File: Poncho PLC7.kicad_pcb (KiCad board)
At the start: 4 copper layers, 135.6 x 54.6 mm, 88 parts, among them J1 TB_1X2, J10 Conn_02x12_Odd_Even, J11 TB_1X2, J12 TB_1X3-PonchoPLC-rescue, J13 Conn_02x05_Odd_Even, J18 Conn_02x05_Odd_Even, J2 TB_1X3-PonchoPLC-rescue, J3 TB_1X2, J4 TB_1X2, J5 TB_1X2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

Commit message: version 3
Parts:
- removed J11, J8: TB_1X2, TerminalBlock_Phoenix:TerminalBlock_Phoenix_MKDS-1,5-2_1x02_P5.00mm_Horizontal
- removed J12: TB_1X3-PonchoPLC-rescue, TerminalBlock_Phoenix:TerminalBlock_Phoenix_MKDS-1,5-3_1x03_P5.00mm_Horizontal
- added JE1: TB_1X2, Poncho-PLC:TerminalBlock_4Ucon_1x02_P3.50mm_Horizontal, F.Cu at (134.0, 105.0)
- added JE2: TB_1X2, Poncho-PLC:TerminalBlock_4Ucon_1x02_P3.50mm_Horizontal, F.Cu at (142.0, 105.0)
- added JE3: TB_1X2, Poncho-PLC:TerminalBlock_4Ucon_1x02_P3.50mm_Horizontal, F.Cu at (150.0, 105.0)
- added JE4: TB_1X3-PonchoPLC-rescue, Poncho-PLC:TerminalBlock_4Ucon_1x03_P3.50mm_Horizontal, F.Cu at (161.5, 105.0)
- added JX1: Conn_02x20_Counter_Clockwise, Poncho-PLC:TX24-40R-LT-H1E, F.Cu at (47.0, 139.5)
- J1, J3, J4, J5, J7: footprint TerminalBlock_Phoenix:TerminalBlock_Phoenix_MKDS-1,5-2_1x02_P5.00mm_Horizontal -> Poncho-PLC:TerminalBlock_4Ucon_1x02_P3.50mm_Horizontal
- J2: footprint TerminalBlock_Phoenix:TerminalBlock_Phoenix_MKDS-1,5-3_1x03_P5.00mm_Horizontal -> Poncho-PLC:TerminalBlock_4Ucon_1x03_P3.50mm_Horizontal
- J9: value TB_1X2 -> Conn_02x12_Odd_Even; footprint TerminalBlock_Phoenix:TerminalBlock_Phoenix_MKDS-1,5-2_1x02_P5.00mm_Horizontal -> Connector_PinSocket_2.54mm:PinSocket_2x12_P2.54mm_Vertical; moved to B.Cu
- moved U5 173.6 mm to (163.6, 138.9), turned to 270 degrees
- moved J3 164.5 mm to (161.8, 150.0)
- moved U6 161.2 mm to (153.2, 138.9), turned to 270 degrees
- moved J5 154.6 mm to (141.0, 150.0)
- moved J4 153.7 mm to (151.5, 150.0)
- moved U7 151.5 mm to (142.8, 138.9), turned to 270 degrees
- moved U8 141.1 mm to (132.3, 138.9), turned to 270 degrees
- moved D8 132.8 mm to (130.0, 130.5), turned to 270 degrees
- moved J7 132.3 mm to (130.6, 150.0)
- moved R13 128.7 mm to (166.2, 130.5), turned to 90 degrees
- moved R9 125.3 mm to (163.8, 130.4), turned to 90 degrees
- moved D5 121.9 mm to (161.5, 130.5), turned to 270 degrees
- moved R10 118.3 mm to (153.0, 130.5), turned to 90 degrees
- moved R14 117.6 mm to (155.5, 130.4), turned to 90 degrees
- moved D6 115.3 mm to (150.8, 130.5), turned to 270 degrees
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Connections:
- net /U1_RX renamed /BaseCIAA7/U1_RX
- net /U1_TX renamed /BaseCIAA7/U1_TX
- J10 pad 10: /PA0 -> /BaseCIAA7/ADC1_INP16
- J10 pad 12: /PA3 -> /BaseCIAA7/ADC12_INP15
- J10 pad 14: /PA4 -> /BaseCIAA7/ADC12_INP18
- J10 pad 16: /PA5 -> /BaseCIAA7/ADC12_INP19
- J10 pad 18: /PA6 -> /BaseCIAA7/ADC12_INP3
- J10 pad 2: /PC13 -> /BaseCIAA7/PC13
- J10 pad 20: /PB1 -> /BaseCIAA7/ADC12_INP5
- J10 pad 22: /PB0 -> /BaseCIAA7/ADC12_INN5_INP9
- J10 pad 4: /PC0 -> /BaseCIAA7/ADC123_INP10
- J10 pad 6: /PC2 -> /BaseCIAA7/ADC12_INN1_INP0
- J10 pad 8: /PC3 -> /BaseCIAA7/ADC3_INP1
- J18 pad 10: VDC -> +5V
- J18 pad 2: VDC -> +5V
- J18 pad 4: VDC -> +5V
- J18 pad 6: VDC -> +5V
- J18 pad 8: VDC -> +5V
- J2 pad 1: Net-(J2-Pad1) -> GND
- J2 pad 3: GND -> Net-(J2-Pad3)
- J6 pad 10: /PD13 -> /BaseCIAA7/IN4
- J6 pad 11: /PD10 -> /BaseCIAA7/IN0
- J6 pad 12: /PD11 -> /BaseCIAA7/IN3
- J6 pad 13: /PD8 -> /BaseCIAA7/OUT3
- J6 pad 14: /PD9 -> /BaseCIAA7/OUT7
- J6 pad 15: /PE15 -> /BaseCIAA7/OUT2
- J6 pad 16: /PB10 -> /BaseCIAA7/OUT6
- J6 pad 17: /PE13 -> /BaseCIAA7/OUT1
- J6 pad 18: /PE14 -> /BaseCIAA7/OUT5
- J6 pad 19: /PE11 -> /BaseCIAA7/OUT0
- J6 pad 20: /PE12 -> /BaseCIAA7/OUT4
- J6 pad 3: /PC9 -> /BaseCIAA7/PC9
- J6 pad 4: /PA8 -> /BaseCIAA7/PA8
- J6 pad 5: /PC6 -> /BaseCIAA7/PC6
- J6 pad 6: /PC7 -> /BaseCIAA7/PC7
- J6 pad 7: /PD14 -> /BaseCIAA7/IN2
- J6 pad 8: /PD15 -> /BaseCIAA7/IN5
- J6 pad 9: /PD12 -> /BaseCIAA7/IN1
- J9 pad 1: Net-(J9-Pad1) -> GND
- J9 pad 2: Net-(J9-Pad2) -> GND
- R21 pad 2: Net-(J9-Pad1) -> Net-(JE2-Pad1)
- R23 pad 2: Net-(J9-Pad2) -> Net-(JE2-Pad2)
- R5 pad 1: Net-(D2-Pad1) -> Net-(D1-Pad1)
- R6 pad 1: Net-(D3-Pad1) -> Net-(D2-Pad1)
- R7 pad 1: Net-(D4-Pad1) -> Net-(D3-Pad1)
- R8 pad 1: Net-(D1-Pad1) -> Net-(D4-Pad1)
- TH1 pad 2: Net-(J1-Pad1) -> Net-(J1-Pad2)
- TH2 pad 2: Net-(J1-Pad2) -> Net-(J1-Pad1)
- TH3 pad 2: Net-(J2-Pad1) -> Net-(J2-Pad3)
- U5 pad 4: Net-(J3-Pad2) -> Net-(J3-Pad1)
- U5 pad 6: Net-(J3-Pad1) -> Net-(J3-Pad2)
- U6 pad 4: Net-(J4-Pad2) -> Net-(J4-Pad1)
- U6 pad 6: Net-(J4-Pad1) -> Net-(J4-Pad2)
- U7 pad 4: Net-(J5-Pad2) -> Net-(J5-Pad1)
- U7 pad 6: Net-(J5-Pad1) -> Net-(J5-Pad2)
- U8 pad 4: Net-(J7-Pad2) -> Net-(J7-Pad1)
- U8 pad 6: Net-(J7-Pad1) -> Net-(J7-Pad2)
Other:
- board text added: "Copyright © 2019 by Agustín Rey"
- board text removed: "LED PC2"
- board text removed: "POWER"

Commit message: Version 4
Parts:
- removed JX1: Conn_02x20_Counter_Clockwise, Poncho-PLC:TX24-40R-LT-H1E
- added  : , Poncho-PLC:Logo_Poncho, F.Cu at (74.4, 136.5)
- added  : , Symbol:OSHW-Logo2_7.3x6mm_Copper, F.Cu at (94.0, 136.6)
- added  : Fiducial, Fiducial:Fiducial_0.5mm_Mask1mm, F.Cu at (43.0, 70.0)
- added  : Fiducial, Fiducial:Fiducial_0.5mm_Mask1mm, F.Cu at (43.0, 134.8)
- added  : Fiducial, Fiducial:Fiducial_0.5mm_Mask1mm, F.Cu at (160.0, 134.8)
- added H5: MountingHole, MountingHole:MountingHole_3.2mm_M3_Pad_Via, F.Cu at (38.0, 65.0)
- added H6: MountingHole, MountingHole:MountingHole_3.2mm_M3_Pad_Via, F.Cu at (38.0, 139.7)
- added H7: MountingHole, MountingHole:MountingHole_3.2mm_M3_Pad_Via, F.Cu at (165.0, 65.0)
- added H8: MountingHole, MountingHole:MountingHole_3.2mm_M3_Pad_Via, F.Cu at (165.0, 139.7)
- added J8: Conn_02x20_Counter_Clockwise, Poncho-PLC:TX24-40R-LT-H1E, F.Cu at (36.5, 114.9)
- D1, D2, D3, D4, D5, D6, D7, D8: footprint LED_SMD:LED_0603_1608Metric -> LED_SMD:LED_0805_2012Metric
- J1: value TB_1X2 -> TB_1X2-PonchoPLC-rescue; footprint Poncho-PLC:TerminalBlock_4Ucon_1x02_P3.50mm_Horizontal -> Poncho-PLC:TerminalBlock_WECO_120-M-311_1x02_P5.00mm_Plug-in_PCB
- J2: footprint Poncho-PLC:TerminalBlock_4Ucon_1x03_P3.50mm_Horizontal -> Poncho-PLC:TerminalBlock_WECO_120-M-311_1x03_P5.00mm_Plug-in_PCB
- J3, J4, J5, JE1, JE2, JE3: footprint Poncho-PLC:TerminalBlock_4Ucon_1x02_P3.50mm_Horizontal -> Poncho-PLC:TerminalBlock_WECO_120-M-311_1x02_P5.00mm_Plug-in_PCB
- J6: value Conn_02x12_Odd_Even -> TB_1X2; footprint Connector_PinSocket_2.54mm:PinSocket_2x12_P2.54mm_Vertical -> Poncho-PLC:TerminalBlock_WECO_120-M-311_1x02_P5.00mm_Plug-in_PCB; moved to F.Cu
- J7: value TB_1X2 -> Conn_02x12_Odd_Even; footprint Poncho-PLC:TerminalBlock_4Ucon_1x02_P3.50mm_Horizontal -> Connector_PinSocket_2.54mm:PinSocket_2x12_P2.54mm_Vertical; moved to B.Cu
- JE4: value TB_1X3-PonchoPLC-rescue -> TB_1X3; footprint Poncho-PLC:TerminalBlock_4Ucon_1x03_P3.50mm_Horizontal -> Poncho-PLC:TerminalBlock_WECO_120-M-311_1x03_P5.00mm_Plug-in_PCB
- R1, R2, R3, R4: value 100k -> 100K
- R17, R19, R21, R23, R25, R27, R29, R31: value 6200 -> 6.2K
- R18, R20, R22, R24, R26, R28, R30, R32: value 2700 -> 2.7K
- moved J7 67.4 mm to (163.0, 90.9), turned to 180 degrees
- moved JE4 56.4 mm to (116.5, 71.0), turned to 0 degrees
- moved J6 52.2 mm to (124.5, 134.0)
- moved C1 50.1 mm to (54.8, 104.0)
- moved R31 49.2 mm to (121.6, 78.3)
- moved R32 49.2 mm to (121.6, 81.8), turned to 270 degrees
- moved R29 43.3 mm to (126.6, 78.3)
- moved R30 43.3 mm to (126.6, 81.8)
- moved C2 42.3 mm to (66.2, 104.0)
- moved R17 41.0 mm to (158.1, 78.3)
- moved R18 41.0 mm to (158.1, 81.8)
- moved R19 40.1 mm to (153.1, 78.3)
- moved R20 40.1 mm to (153.1, 81.8), turned to 270 degrees
- moved C9 40.0 mm to (150.5, 95.0)
- moved JE1 38.9 mm to (153.0, 71.0), turned to 0 degrees
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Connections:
- J6 pad 1: /BaseCIAA7/U1_TX -> Net-(J6-Pad1)
- J6 pad 2: /BaseCIAA7/U1_RX -> Net-(J6-Pad2)
- J7 pad 1: Net-(J7-Pad1) -> /BaseCIAA7/U1_TX
- J7 pad 2: Net-(J7-Pad2) -> /BaseCIAA7/U1_RX
- R17 pad 2: Net-(JE1-Pad1) -> Net-(JE1-Pad2)
- R19 pad 2: Net-(JE1-Pad2) -> Net-(JE1-Pad1)
- R21 pad 2: Net-(JE2-Pad1) -> Net-(JE2-Pad2)
- R23 pad 2: Net-(JE2-Pad2) -> Net-(JE2-Pad1)
- R25 pad 2: Net-(JE3-Pad1) -> Net-(JE3-Pad2)
- R27 pad 2: Net-(JE3-Pad2) -> Net-(JE3-Pad1)
- U5 pad 4: Net-(J3-Pad1) -> Net-(J3-Pad2)
- U5 pad 6: Net-(J3-Pad2) -> Net-(J3-Pad1)
- U6 pad 4: Net-(J4-Pad1) -> Net-(J4-Pad2)
- U6 pad 6: Net-(J4-Pad2) -> Net-(J4-Pad1)
- U7 pad 4: Net-(J5-Pad1) -> Net-(J5-Pad2)
- U7 pad 6: Net-(J5-Pad2) -> Net-(J5-Pad1)
- U8 pad 4: Net-(J7-Pad1) -> Net-(J6-Pad2)
- U8 pad 6: Net-(J7-Pad2) -> Net-(J6-Pad1)
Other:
- board size 135.6 x 54.6 mm -> 135.6 x 83.3 mm
- copper layers 4 -> 2
- net class Default: clearance 0.2 -> 0.3; trace_width 0.25 -> 0.5; via_dia 0.8 -> 1.5; via_drill 0.4 -> 0.7
- net class Delgadas added: clearance 0.3, trace_width 0.3, via_dia 1, via_drill 0.5
- net class Potencia added: clearance 0.3, trace_width 1, via_dia 1, via_drill 0.5
- rule trace_clearance: 0.2 -> 0.3
- rule trace_min: 0.2 -> 0.3
- rule via_min_drill: 0.3 -> 0.5
- rule via_min_size: 0.4 -> 1
- board text added: "Ancho mínimo de pista: 0,25mm Separacion mínima entre pistas: 0,25mm Diametro mínimo de via: 1mm Perforación mínima de via: 0,5m Material de fabricación: FR-4 - 1,6mm Espesor de cobre 35um / 1oz Doble faz con orificios metalizados Terminación superficial SnPb HASL"
- board text added: "Grilla de posicionamiento: Principal 0,5mm Alternativa 0,25mm Grilla de ruteo: Principal 0,5mm Alternativa 0,25mm Referencia: Ernesto Mayer, Estándar 10 mils"
- board text added: "Información de diseño"
- board text added: "Información de fabricación"
- board text removed: "Copyright © 2019 by Agustín Rey"

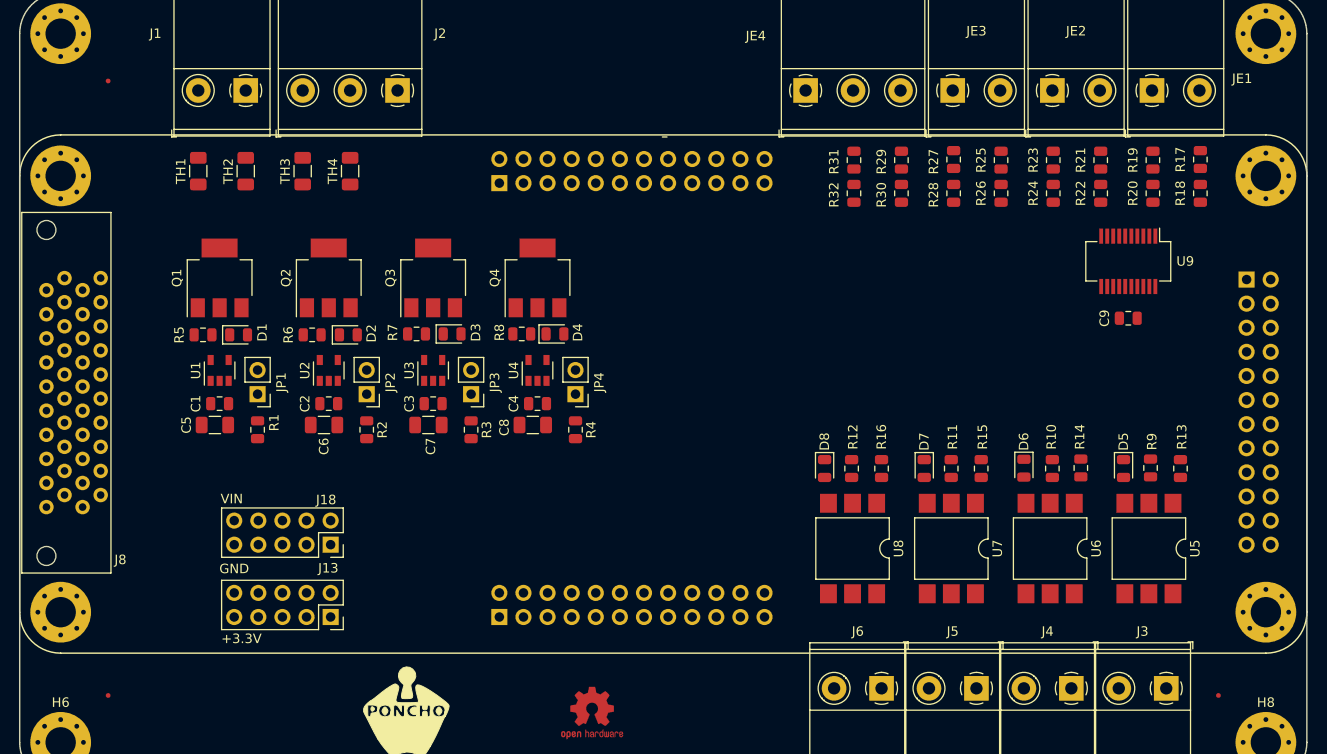
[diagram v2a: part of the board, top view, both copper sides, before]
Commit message: Ruteo Parcial-Replanteo Esquematico pafa favorecer ruteo
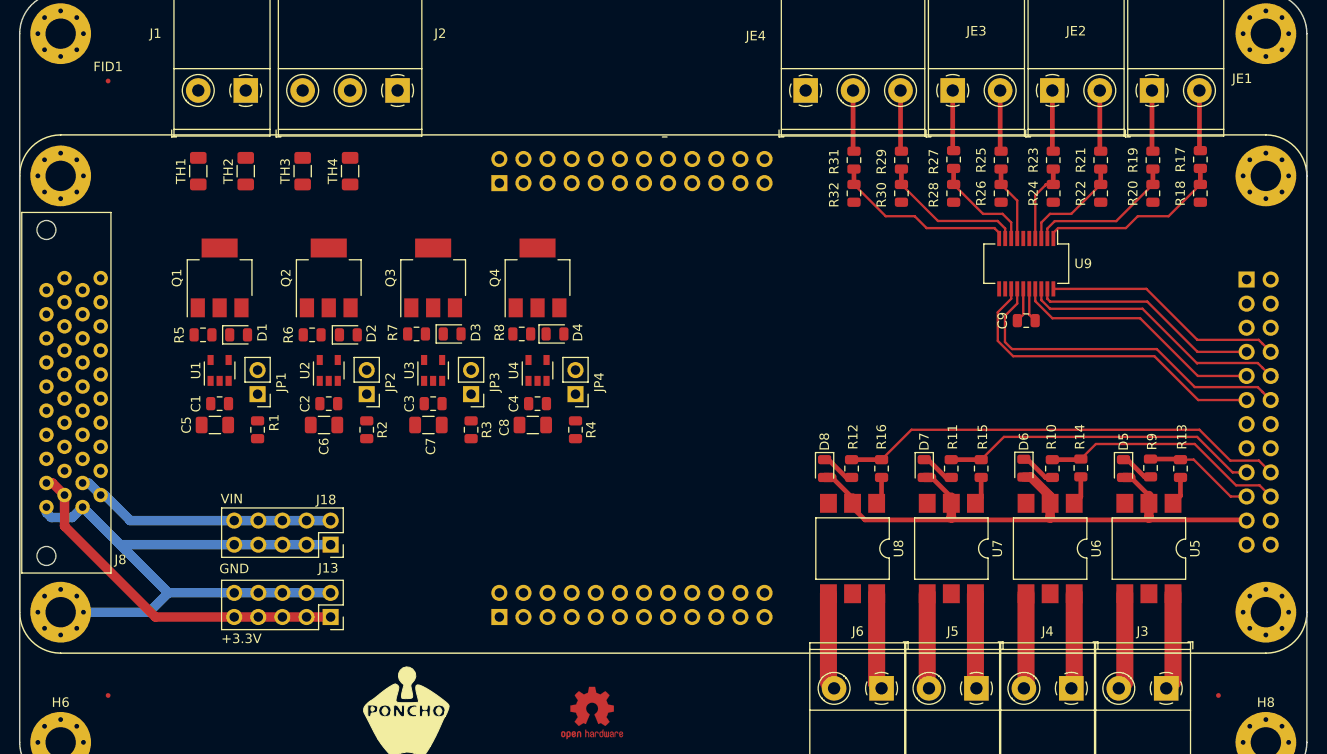
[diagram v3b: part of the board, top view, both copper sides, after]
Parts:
- FID1, FID2, FID3: renamed from  
- moved C9 10.8 mm to (139.8, 95.2)
- moved U9 10.8 mm to (139.8, 89.2)
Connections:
- net Net-(R17-Pad1) renamed /Entradas/A1
- net Net-(R19-Pad1) renamed /Entradas/A2
- net Net-(R21-Pad1) renamed /Entradas/A3
- net Net-(R23-Pad1) renamed /Entradas/A4
- net Net-(R25-Pad1) renamed /Entradas/A5
- net Net-(R27-Pad1) renamed /Entradas/A6
- net Net-(R29-Pad1) renamed /Entradas/A7
- net Net-(R31-Pad1) renamed /Entradas/A8
- J7 pad 10: /BaseCIAA7/IN4 -> /BaseCIAA7/IN2
- J7 pad 11: /BaseCIAA7/IN0 -> /BaseCIAA7/IN5
- J7 pad 12: /BaseCIAA7/IN3 -> /BaseCIAA7/IN4
- J7 pad 14: /BaseCIAA7/OUT7 -> /BaseCIAA7/OUT0
- J7 pad 16: /BaseCIAA7/OUT6 -> /BaseCIAA7/OUT1
- J7 pad 17: /BaseCIAA7/OUT1 -> /BaseCIAA7/OUT6
- J7 pad 18: /BaseCIAA7/OUT5 -> /BaseCIAA7/OUT7
- J7 pad 19: /BaseCIAA7/OUT0 -> /BaseCIAA7/OUT4
- J7 pad 20: /BaseCIAA7/OUT4 -> /BaseCIAA7/OUT5
- J7 pad 7: /BaseCIAA7/IN2 -> /BaseCIAA7/IN1
- J7 pad 8: /BaseCIAA7/IN5 -> /BaseCIAA7/IN0
- J7 pad 9: /BaseCIAA7/IN1 -> /BaseCIAA7/IN3
- J8 pad 2: +5V -> +3V3
- J8 pad 31: +3V3 -> +5V
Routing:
- net GND: track 0.00 -> 138.0 mm
- net /BaseCIAA7/OUT7: track 0.00 -> 47.3 mm
- net +3V3: track 0.00 -> 41.3 mm
- net /BaseCIAA7/IN4: track 0.00 -> 36.7 mm
- net /BaseCIAA7/IN5: track 0.00 -> 34.9 mm
- net /BaseCIAA7/OUT6: track 0.00 -> 33.7 mm
- net /BaseCIAA7/IN2: track 0.00 -> 28.7 mm
- net +5V: track 0.00 -> 27.8 mm
- net /BaseCIAA7/IN3: track 0.00 -> 26.8 mm
- net /BaseCIAA7/OUT5: track 0.00 -> 26.0 mm
- net /BaseCIAA7/IN0: track 0.00 -> 25.6 mm
- net /BaseCIAA7/IN1: track 0.00 -> 24.4 mm
- net /Entradas/A1: track 0.00 -> 19.9 mm
- net /Entradas/A8: track 0.00 -> 19.6 mm
- net /Entradas/A2: track 0.00 -> 15.7 mm
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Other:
- net class FinePitch added: clearance 0.2, trace_width 0.25, via_dia 1.5, via_drill 0.7
- rule trace_min: 0.3 -> 0.25

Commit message: Ruteo Parcial-Replanteo Esquematico pafa favorecer ruteo v4
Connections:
- J7 pad 13: /BaseCIAA7/OUT3 -> /BaseCIAA7/OUT2
- J7 pad 14: /BaseCIAA7/OUT0 -> /BaseCIAA7/OUT3
- J7 pad 15: /BaseCIAA7/OUT2 -> /BaseCIAA7/OUT0
- J8 pad 18: /BaseCIAA7/PD5 -> /BaseCIAA7/PB5
- J8 pad 28: /BaseCIAA7/PA15 -> /BaseCIAA7/PD3
- J8 pad 8: /BaseCIAA7/PD3 -> /BaseCIAA7/PA15
- J8 pad 9: /BaseCIAA7/PB5 -> /BaseCIAA7/PD5
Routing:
- net GND: track 138.0 -> 338.1 mm, vias 0 -> 9
- net /BaseCIAA7/OUT0: track 0.00 -> 119.6 mm
- net /BaseCIAA7/OUT1: track 0.00 -> 110.9 mm
- net /BaseCIAA7/OUT2: track 0.00 -> 96.7 mm
- net /BaseCIAA7/PA15: track 0.00 -> 87.2 mm
- net /BaseCIAA7/OUT3: track 0.00 -> 82.0 mm
- net /BaseCIAA7/PD4: track 0.00 -> 79.8 mm, vias 0 -> 1
- net /BaseCIAA7/PD5: track 0.00 -> 79.5 mm
- net /BaseCIAA7/PC10: track 0.00 -> 79.4 mm
- net /BaseCIAA7/PD3: track 0.00 -> 78.3 mm
- net GNDREF: track 0.00 -> 72.9 mm, vias 0 -> 9
- net /BaseCIAA7/PB5: track 0.00 -> 71.8 mm, vias 0 -> 1
- net /BaseCIAA7/PD6: track 0.00 -> 71.5 mm
- net /BaseCIAA7/PB3: track 0.00 -> 70.4 mm
- net /BaseCIAA7/PB4: track 0.00 -> 69.6 mm
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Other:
- net class UltraFinePitch added: clearance 0.18, trace_width 0.2, via_dia 1.5, via_drill 0.7
- rule trace_min: 0.25 -> 0.2
- board text added: "Grilla de posicionamiento: Principal 0,5mm Alternativa 0,25mm Nota: en J8 algunas pistas utilizan 0.2mm con clearance de 0.2mm Grilla de ruteo: Principal 0,5mm Alternativa 0,25mm Referencia: Ernesto Mayer, Estándar 10 mils Nota: en J8 hay algunas zonas con estándar 8 mils"
- board text removed: "Grilla de posicionamiento: Principal 0,5mm Alternativa 0,25mm Grilla de ruteo: Principal 0,5mm Alternativa 0,25mm Referencia: Ernesto Mayer, Estándar 10 mils"
